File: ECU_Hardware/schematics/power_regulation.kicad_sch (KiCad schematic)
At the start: 24 parts, among them U2 LMR38020SQDDARQ1, U5 LM66200DRLR, U6 AP2112K-3.3

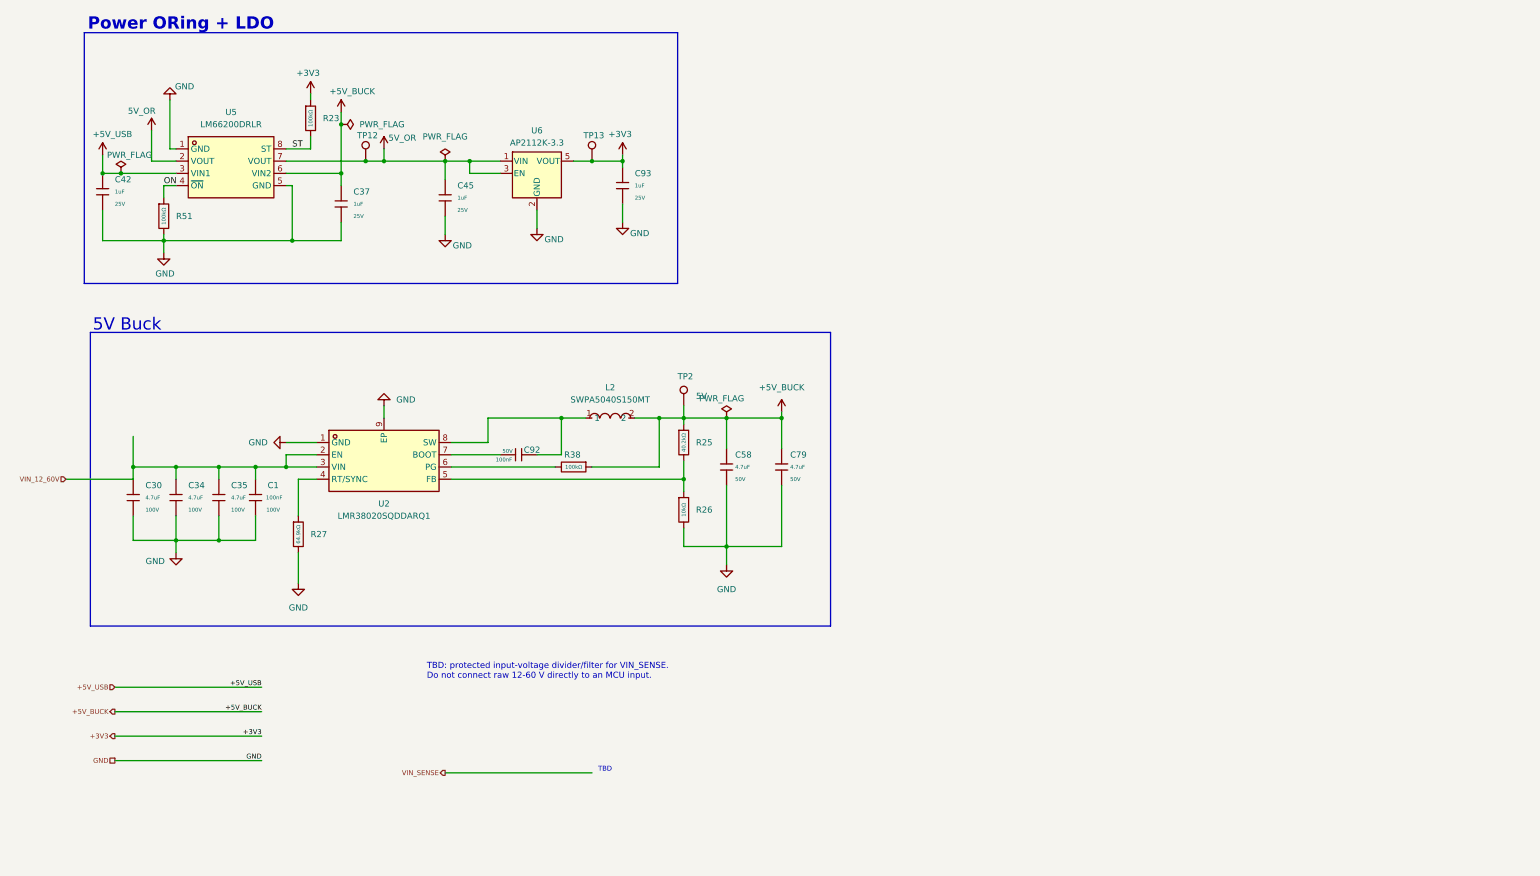
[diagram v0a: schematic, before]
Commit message: Move ECU schematics into schematics/ and add driver inputs and sensor notes
Hierarchical sheets now live in ECU_Hardware/schematics, with the new
Driver_Inputs sheet (APPS, BPPS and steering dividers and clamps), the
reviewed and JLCPCB project symbol libraries, new 3D models, and
SENSOR_INTERFACES.md with the GPS, IMU and temperature pin allocation.
The old top-level sheets and the restore backup are removed.

Claude-Session: https://claude.ai/code/session_0117trEbCv7z6CPYkN3K3GKQ
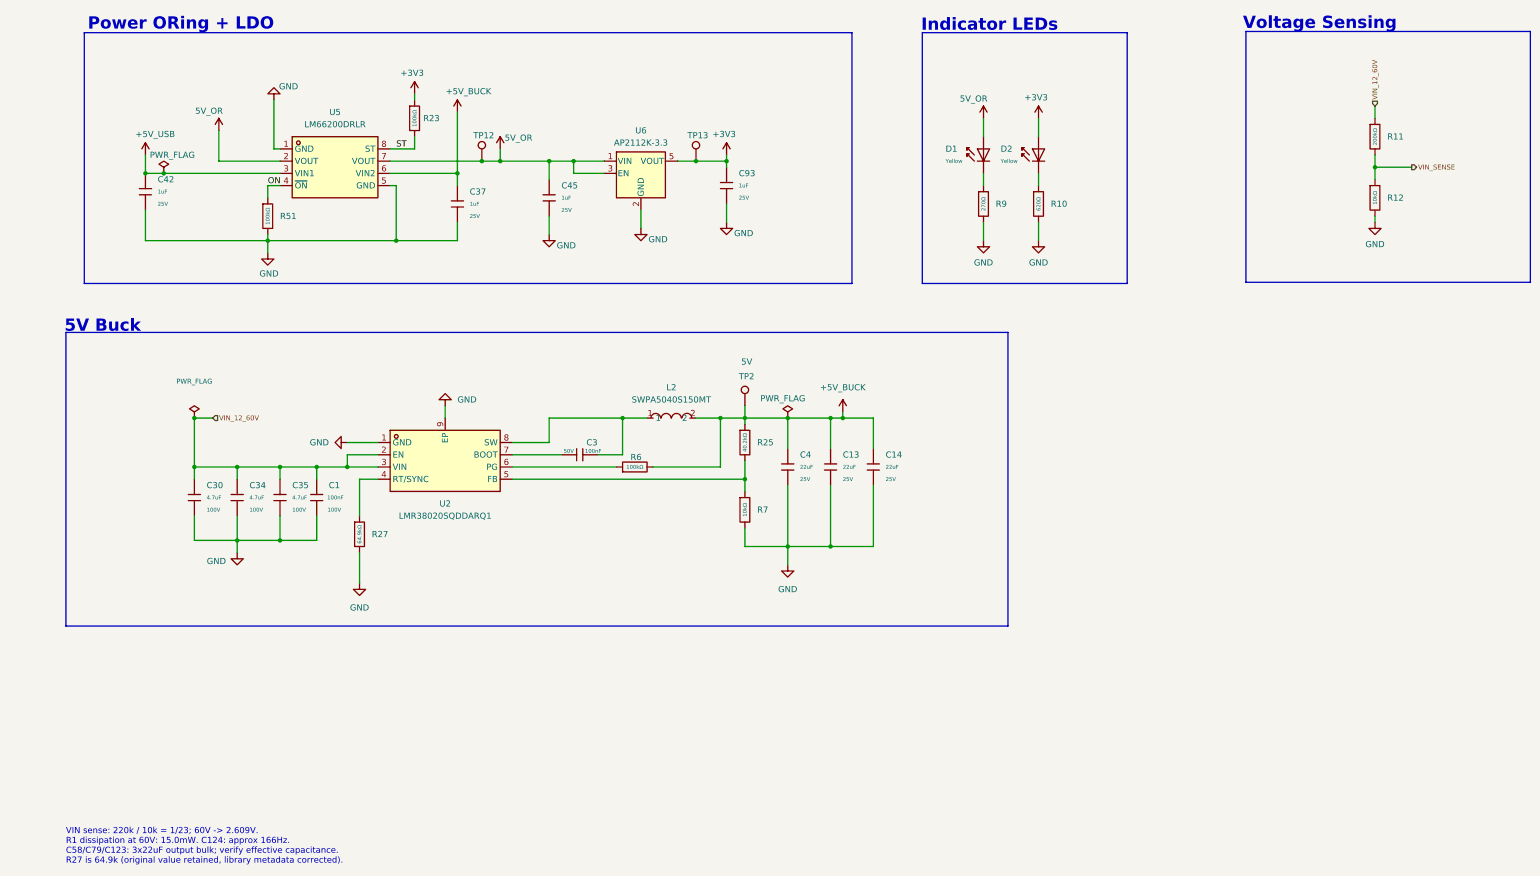
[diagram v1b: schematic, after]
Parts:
- removed C58, C79: 4.7uF, PCM_JLCPCB:C_0805, symbol PCM_JLCPCB-Capacitors:0805,4.7uF
- removed C92: 100nF, PCM_JLCPCB:C_0603, symbol PCM_JLCPCB-Capacitors:0603,100nF
- removed R26: 10kΩ, PCM_JLCPCB:R_0603, symbol PCM_JLCPCB-Resistors:0603,10kΩ
- removed R38: 100kΩ, PCM_JLCPCB:R_0805, symbol JLCLCSC_SYMBOLS_LIB:0805,100kΩ
- added C13, C14, C4: 22uF, PCM_JLCPCB:C_0805, symbol PCM_JLCPCB-Capacitors:0805,22uF
- added C3: 100nF, PCM_JLCPCB:C_0402, symbol PCM_JLCPCB-Capacitors:0402,100nF,(2)
- added D1, D2: Yellow, PCM_JLCPCB:D_0805, symbol PCM_JLCPCB-Diodes:LED,0805,Yellow
- added R10: 620Ω, PCM_JLCPCB:R_0603, symbol PCM_JLCPCB-Resistors:0603,620Ω
- added R11: 200kΩ, PCM_JLCPCB:R_0603, symbol PCM_JLCPCB-Resistors:0603,200kΩ
- added R12: 10kΩ, PCM_JLCPCB:R_0603, symbol PCM_JLCPCB-Resistors:0603,10kΩ
- added R6: 100kΩ, PCM_JLCPCB:R_0402, symbol PCM_JLCPCB-Resistors:0402,100kΩ
- added R7: 10kΩ, PCM_JLCPCB:R_0402, symbol PCM_JLCPCB-Resistors:0402,10kΩ
- added R9: 270Ω, PCM_JLCPCB:R_0603, symbol PCM_JLCPCB-Resistors:0603,270Ω
- L2: symbol easyeda2kicad:SWPA5040S150MT -> ECU_Reviewed:SWPA5040S150MT
- R27: footprint PCM_JLCPCB:R_0603 -> PCM_JLCPCB:R_0402; Attrition Qty (none) -> 10; LCSC C14891 -> C5713275; Manufacturer UNI-ROYAL(Uniroyal Elec) -> FOJAN; Minimum Qty (none) -> 20; Overload Voltage (Max) 75V -> 50V; Part 0603WAF6492T5E -> FRC0402F6492TS; Power(Watts) 100mW -> 62.5mW
- U2: symbol easyeda2kicad:LMR38020SQDDARQ1 -> ECU_Reviewed:LMR38020SQDDARQ1
- U5: symbol easyeda2kicad:LM66200DRLR -> ECU_Reviewed:LM66200DRLR
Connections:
- net +3V3: now also D2.2
- net +5V_BUCK: now also C13.1, C14.1, C4.1, R6.2
- net 5V_OR: now also D1.2
- net GND: now also C13.2, C14.2, C4.2, R10.2, R12.2, R7.2, R9.2
- net VIN_12_60V: now also R11.1
- net VIN_SENSE: now also R11.2, R12.1
- net at L2.1, U2.8 (SW): now also C3.2
- net at U2.7 (BOOT): now also C3.1
- net at U2.6 (PG): now also R6.1
- net at R25.2, U2.5 (FB): now also R7.1
- new net: D2.1, R10.1
- new net: D1.1, R9.1
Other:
- note added: "Indicator LEDs"
- note added: "VIN sense: 220k / 10k = 1/23; 60V -> 2.609V. R1 dissipation at 60V: 15.0mW. C124: approx 166Hz. C58/C79/C123: 3x22uF output bulk; verify effective capacitance. R27 is 64.9k (original value retained, library metadata corrected)."
- note added: "Voltage Sensing"
- note removed: "TBD"
- note removed: "TBD: protected input-voltage divider/filter for VIN_SENSE. Do not connect raw 12-60 V directly to an MCU input."
- moved on the sheet: C1, C30, C34, C35, C37, C42, C45, C93, L2, R23, R25, R51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
